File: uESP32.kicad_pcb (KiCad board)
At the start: 2 copper layers, 20.3 x 26.7 mm, 26 parts, among them J1 USB_B_Micro, J2 Conn_01x14, J3 Conn_01x14, J4 Conn_01x10, J5 Conn_01x02, Q1 MMBT2222, Q2 MMBT2222, Q3 Si2323, U1 ESP32-WROOM-32, U2 CP2104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

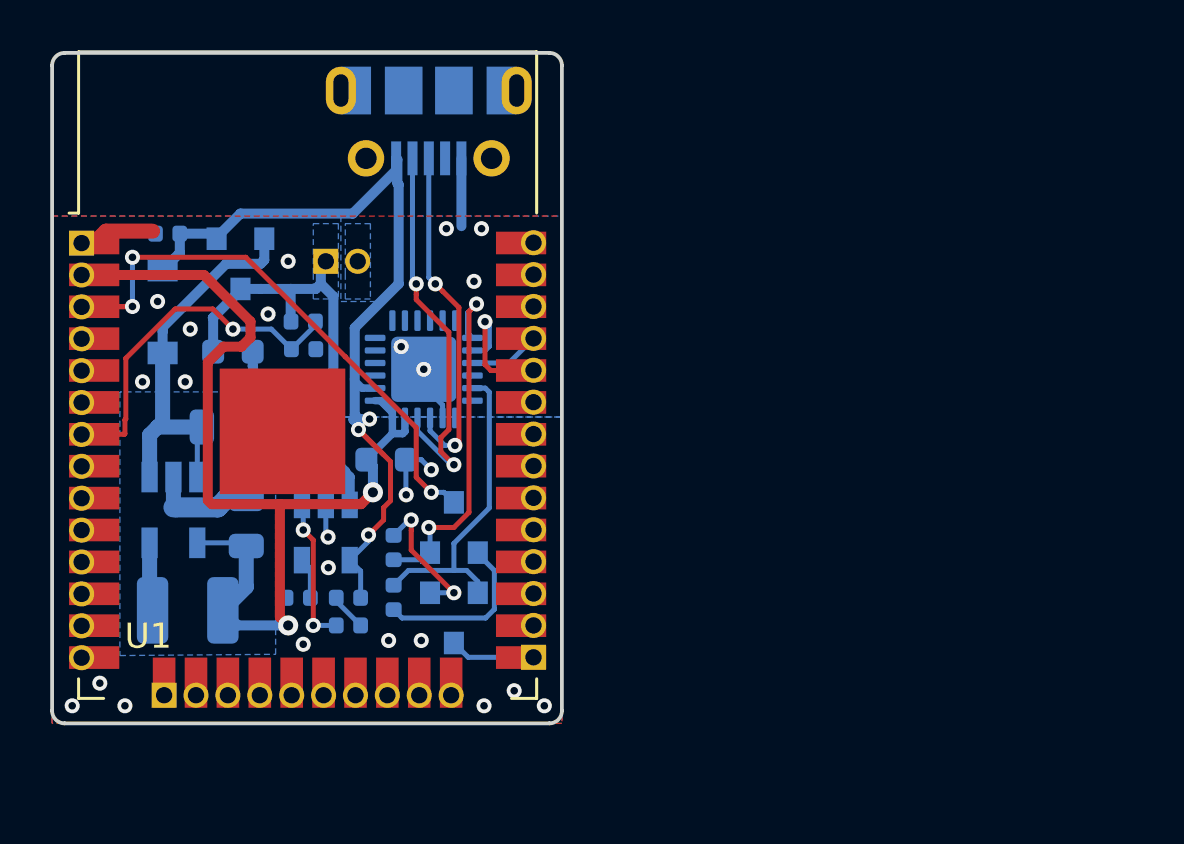
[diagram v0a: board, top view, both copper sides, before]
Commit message: version 2 2.54 pin header
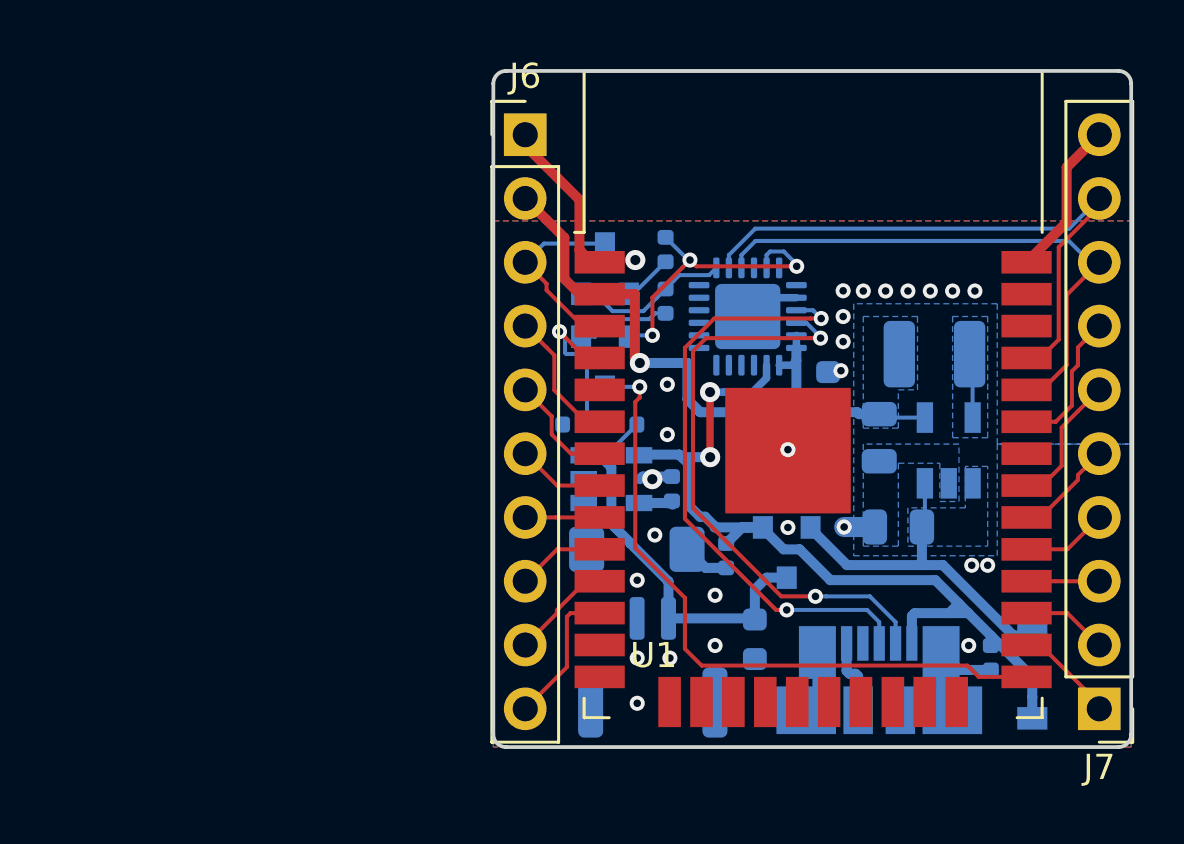
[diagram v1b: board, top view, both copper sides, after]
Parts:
- removed J2, J3: Conn_01x14, Connector_PinHeader_1.27mm:PinHeader_1x14_P1.27mm_Vertical
- removed J4: Conn_01x10, Connector_PinHeader_1.27mm:PinHeader_1x10_P1.27mm_Vertical
- added J6: Conn_01x10, Connector_PinHeader_2.54mm:PinHeader_1x10_P2.54mm_Vertical, F.Cu at (91.4, 48.3)
- added J7: Conn_01x10, Connector_PinHeader_2.54mm:PinHeader_1x10_P2.54mm_Vertical, F.Cu at (114.3, 71.1)
- D2: footprint LED_SMD:LED_0402_1005Metric -> LED_SMD:LED_1806_4516Metric
- J1: footprint Connector_USB:USB_Micro-B_Molex-105017-0001 -> Connector_USB:USB_Micro-B_Molex_47346-0001
- J5: footprint Connector_PinHeader_1.27mm:PinHeader_1x02_P1.27mm_Vertical -> Connector_JST:JST_GH_BM02B-GHS-TBT_1x02-1MP_P1.25mm_Vertical
- moved D1 37.6 mm to (111.6, 69.8), turned to 270 degrees
- moved R4 36.9 mm to (110.0, 69.1), turned to 270 degrees
- moved L1 31.4 mm to (107.7, 57.0), turned to 180 degrees
- moved U4 31.0 mm to (108.3, 60.8), turned to 90 degrees
- moved J1 28.6 mm to (105.5, 70.0), turned to 180 degrees
- moved C3 27.1 mm to (106.3, 63.9), turned to 180 degrees
- moved C4 25.4 mm to (105.5, 60.3), turned to 270 degrees
- moved Q3 24.6 mm to (101.9, 64.9)
- moved C2 23.7 mm to (100.6, 68.4), turned to 270 degrees
- moved J5 20.8 mm to (96.5, 69.5), turned to 0 degrees
- moved U1 20.1 mm to (102.9, 61.6)
- moved C1 17.8 mm to (103.5, 58.5), turned to 90 degrees
- moved R2 17.6 mm to (97.0, 52.8)
- moved R3 15.5 mm to (97.3, 62.4), turned to 270 degrees
- moved R5 15.1 mm to (99.4, 65.0), turned to 270 degrees
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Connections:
- J5 pad 1: +BATT -> GND
- J5 pad 2: GND -> +BATT
- R6 pad 2: IO35 -> SENSOR_VP
- R7 pad 1: IO35 -> SENSOR_VP
- U1 pad 39: (no net) -> GND
- U2 pad 20: RXD0 -> TXD0
- U2 pad 21: TXD0 -> RXD0
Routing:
- net IO0: track 3.41 -> 26.8 mm, vias 0 -> 1
- net TXD0: track 2.84 -> 24.1 mm
- net RXD0: track 5.04 -> 22.0 mm, vias 1 -> 0
- net RESET: track 22.7 -> 7.65 mm, vias 3 -> 0
- net +3V3: track 41.0 -> 26.7 mm, vias 2 -> 1
- net Net-(J1-Pad3): track 13.7 -> 24.1 mm
- net IO35: track 13.8 -> 4.44 mm, vias 1 -> 0
- net RTS: track 14.4 -> 6.38 mm, vias 2 -> 0
- net Net-(J1-Pad2): track 15.7 -> 23.6 mm
- net SENSOR_VP: track 0.00 -> 7.57 mm, vias 0 -> 1
- net IO27: track 0.00 -> 5.72 mm
- net IO21: track 0.00 -> 5.69 mm
- net IO19: track 0.00 -> 5.37 mm
- net IO34: track 0.00 -> 5.36 mm
- net Net-(Q2-Pad1): track 6.82 -> 1.99 mm
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- added copper zone on B.Cu, net +3V3
- added copper zone on B.Cu, net Net-(C3-Pad1)
- added copper zone on B.Cu, net Net-(L1-Pad1)
- removed copper zone on B.Cu, net +BATT
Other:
- board size 20.3 x 26.7 mm -> 25.4 x 26.9 mm
- board text added: "v2.0"
- board text removed: "v1.0"
